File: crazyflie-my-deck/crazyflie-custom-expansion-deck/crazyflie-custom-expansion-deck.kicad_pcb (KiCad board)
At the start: 2 copper layers, 28 x 16 mm, 3 parts, among them J1 Conn_01x10, J2 Conn_02x10_Odd_Even, J3 Conn_01x10

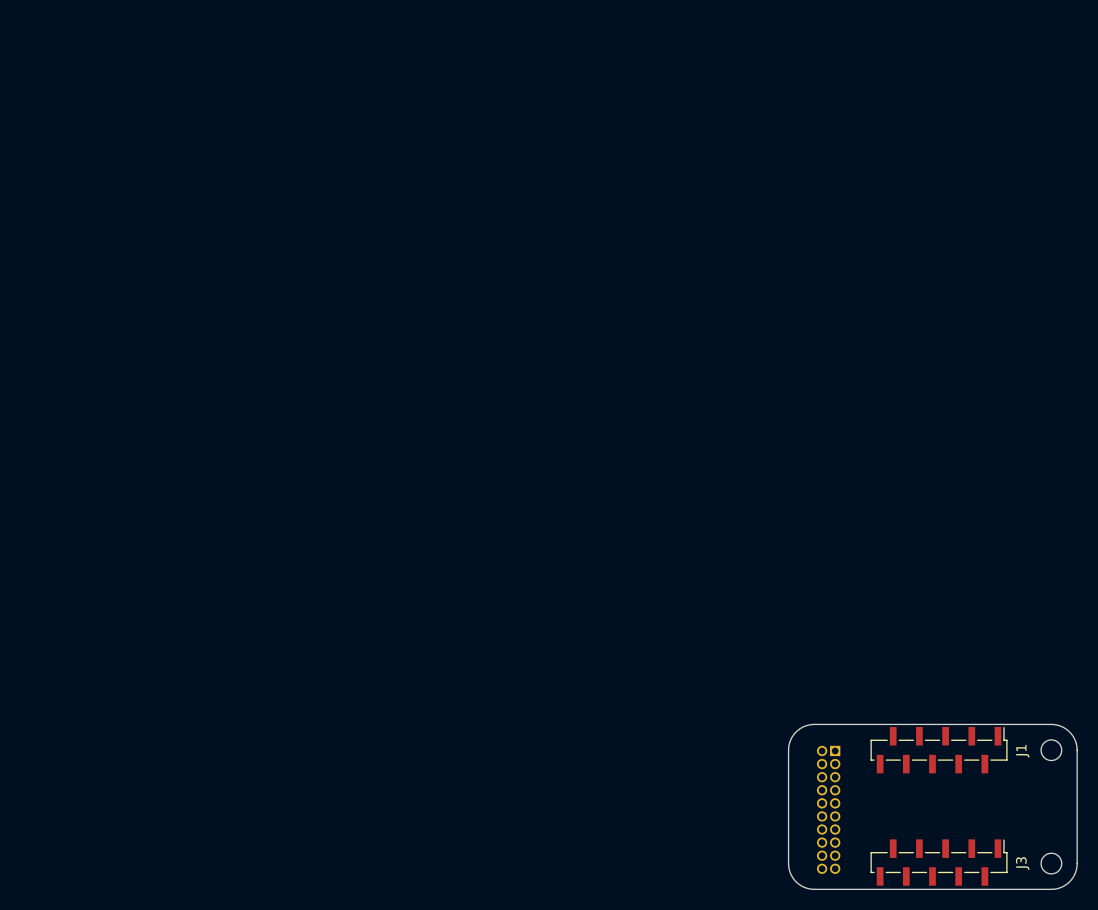
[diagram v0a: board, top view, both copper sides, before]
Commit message: [add] boost voltage
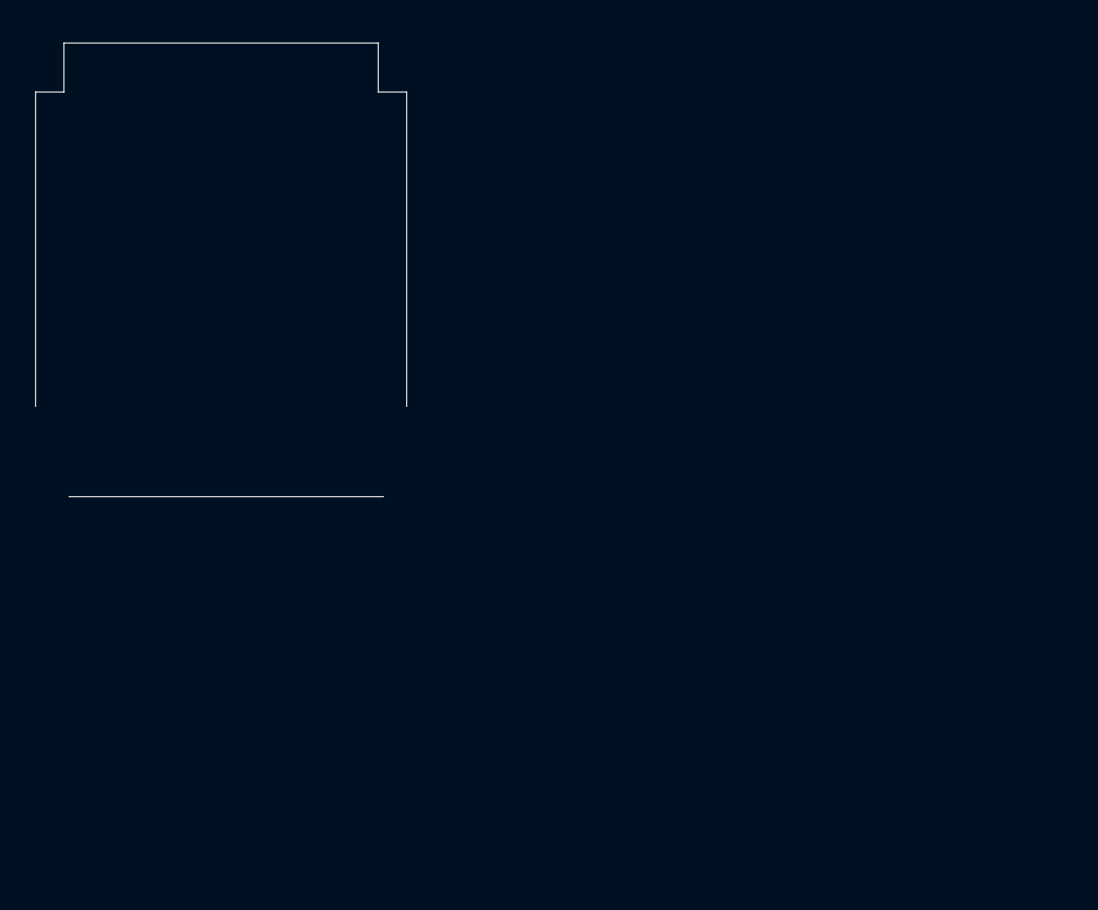
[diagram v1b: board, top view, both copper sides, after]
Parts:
- removed J1, J3: Conn_01x10, Connector_PinSocket_1.27mm:PinSocket_1x10_P1.27mm_Vertical_SMD_Pin1Left
- removed J2: Conn_02x10_Odd_Even, Connector_PinHeader_1.27mm:PinHeader_2x10_P1.27mm_Vertical
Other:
- board size 28 x 16 mm -> 36 x 44 mm

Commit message: acomodo de componentes
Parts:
- added C1: C_Polarized, Capacitor_Tantalum_SMD:CP_EIA-3528-15_AVX-H, F.Cu at (63.8, 35.0)
- added C2: C_Polarized, Capacitor_SMD:C_0805_2012Metric, F.Cu at (82.7, 52.0)
- added C3: C_Polarized, Capacitor_SMD:C_1210_3225Metric, F.Cu at (62.2, 52.0)
- added C4: C_Polarized, Capacitor_Tantalum_SMD:CP_EIA-3528-15_AVX-H, F.Cu at (77.5, 35.2)
- added D1: 1SS355VM, Diode_SMD:D_SOD-323F, F.Cu at (76.2, 40.0)
- added J1: Conn_01x10, Connector_PinSocket_1.27mm:PinSocket_1x10_P1.27mm_Vertical_SMD_Pin1Left, F.Cu at (56.8, 41.5)
- added J2: Conn_01x06_Male, Connector_PinHeader_1.27mm:PinHeader_1x06_P1.27mm_Horizontal, F.Cu at (68.2, 29.7)
- added J3: Conn_01x10, Connector_PinSocket_1.27mm:PinSocket_1x10_P1.27mm_Vertical_SMD_Pin1Left, F.Cu at (83.5, 41.5)
- added L1: L, Inductor_SMD:L_1210_3225Metric, F.Cu at (70.8, 34.8)
- added R1: R, Resistor_SMD:R_0805_2012Metric, F.Cu at (62.7, 40.5)
- added R2: R, Resistor_SMD:R_0805_2012Metric, F.Cu at (62.5, 43.5)
- added R3: R, Resistor_SMD:R_0805_2012Metric, F.Cu at (77.7, 49.2)
- added R4: R, Resistor_SMD:R_0805_2012Metric, F.Cu at (77.8, 51.8)
- added U1: MAX712CSE, Package_SO:SOIC-16_3.9x9.9mm_P1.27mm, F.Cu at (70.0, 43.0)
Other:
- board size 36 x 44 mm -> 36.2 x 37.7 mm

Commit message: Fixes
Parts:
- C1, C4: value C_Polarized -> 100uF
- C2: value C_Polarized -> 0.1uF
- C3: value C_Polarized -> 10uF
- R1: value R -> 120k
- R2: value R -> 30k
- R3: value R -> 390k
- R4: value R -> 130k
- U1: value MAX712CSE -> MAX7111
- moved C2 9.04 mm to (76.2, 45.7), turned to 90 degrees
- moved R3 7.74 mm to (73.7, 55.9), turned to -90 degrees
- moved R2 4.76 mm to (62.5, 48.3)
- moved R4 4.25 mm to (78.7, 55.9), turned to 90 degrees
- moved U1 3.07 mm to (68.6, 45.7)
- moved C3 2.41 mm to (62.2, 54.4)
- moved R1 1.71 mm to (61.0, 40.6)
- moved D1 0.64 mm to (76.2, 40.6)
- moved J2 0.35 mm to (68.6, 29.7)
- renumbered L1 to 22uH1
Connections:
- 22uH1 pad 2: Net-(D1-Pad2) -> Net-(22uH1-Pad2)
- C2 pad 1: unconnected-(C2-Pad1) -> Net-(C2-Pad1)
- C3 pad 1: unconnected-(C3-Pad1) -> Net-(C3-Pad1)
- D1 pad 2: Net-(D1-Pad2) -> Net-(22uH1-Pad2)
- R3 pad 1: unconnected-(R3-Pad1) -> Net-(C3-Pad1)
- U1 pad 1: unconnected-(U1-Pad1) -> Net-(22uH1-Pad2)
- U1 pad 10: unconnected-(U1-Pad10) -> Net-(C2-Pad1)
- U1 pad 11: unconnected-(U1-Pad11) -> Net-(R1-Pad2)
- U1 pad 12: unconnected-(U1-Pad12) -> Net-(C4-Pad1)
- U1 pad 13: unconnected-(U1-Pad13) -> Net-(C2-Pad1)
- U1 pad 14: unconnected-(U1-Pad14) -> GND
- U1 pad 15: unconnected-(U1-Pad15) -> GND
- U1 pad 16: unconnected-(U1-Pad16) -> Net-(22uH1-Pad2)
- U1 pad 2: unconnected-(U1-Pad2) -> GND
- U1 pad 3: unconnected-(U1-Pad3) -> GND
- U1 pad 4: unconnected-(U1-Pad4) -> Net-(C4-Pad1)
- U1 pad 5: unconnected-(U1-Pad5) -> Net-(C4-Pad1)
- U1 pad 6: unconnected-(U1-Pad6) -> Net-(R3-Pad2)
- U1 pad 7: unconnected-(U1-Pad7) -> Net-(C4-Pad1)
- U1 pad 9: unconnected-(U1-Pad9) -> Net-(C3-Pad1)
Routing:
- net GND: track 0.00 -> 26.9 mm
- net Net-(R1-Pad2): track 0.00 -> 10.6 mm
- net Net-(C3-Pad1): track 0.00 -> 7.04 mm
- net Net-(22uH1-Pad1): track 0.00 -> 6.54 mm
- net Net-(R3-Pad2): track 0.00 -> 5.08 mm

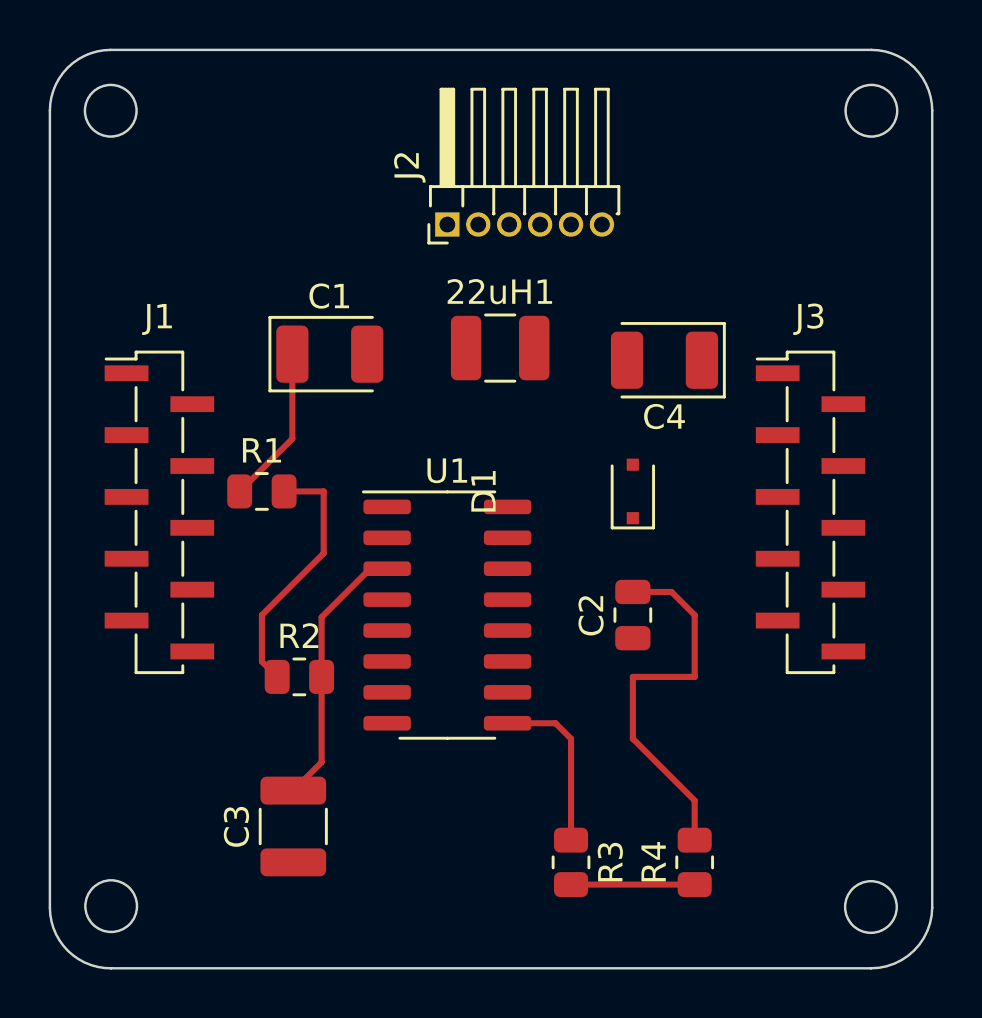
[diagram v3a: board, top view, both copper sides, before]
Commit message: Tracks - voltage boost
Falta 1 y las tracks a GND
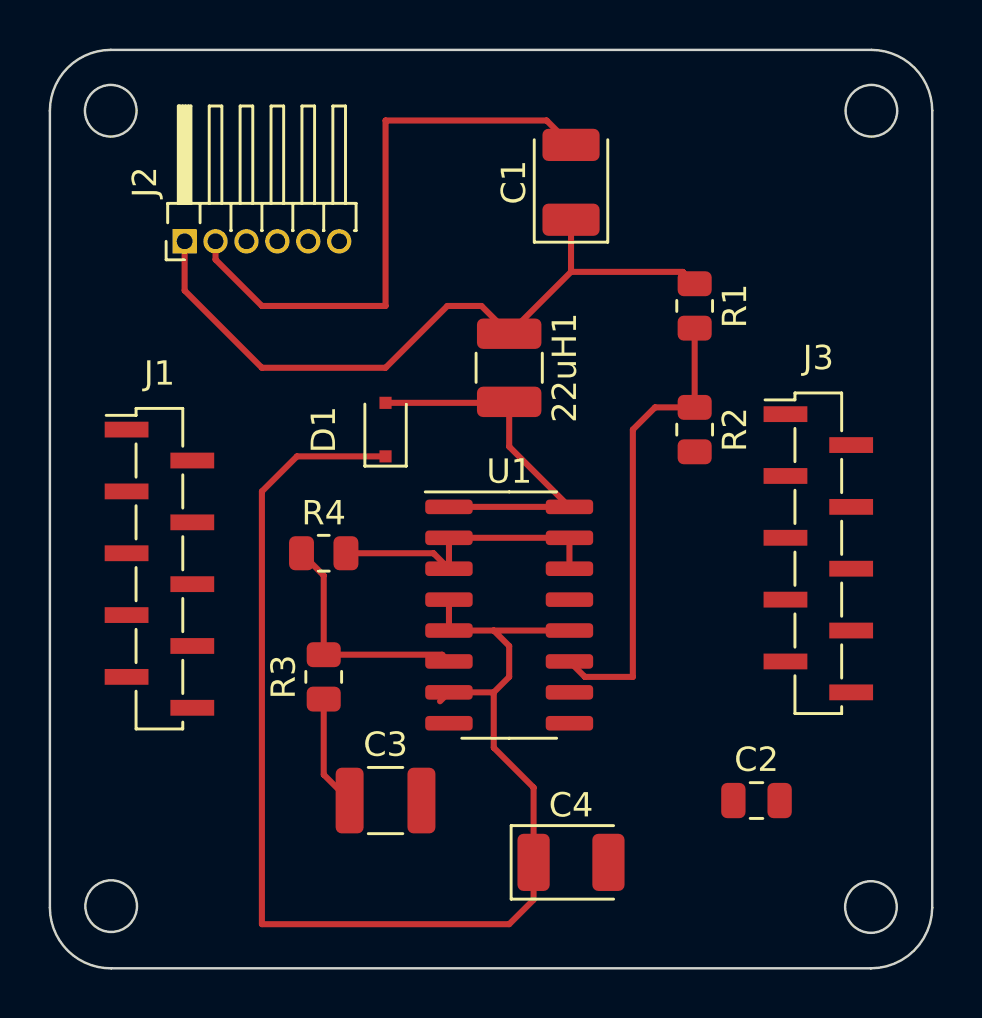
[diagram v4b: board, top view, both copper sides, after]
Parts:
- moved C4 21.0 mm to (73.7, 55.9), turned to 0 degrees
- moved R4 19.8 mm to (63.5, 43.2), turned to 0 degrees
- moved R1 19.3 mm to (78.7, 33.0), turned to -90 degrees
- moved R2 19.2 mm to (78.7, 38.1), turned to -90 degrees
- moved R3 12.7 mm to (63.5, 48.3), turned to 90 degrees
- moved C1 12.2 mm to (73.7, 27.9), turned to 90 degrees
- moved J2 10.8 mm to (57.8, 30.4)
- moved D1 10.5 mm to (66.0, 38.1)
- moved C2 9.16 mm to (81.3, 53.3), turned to 0 degrees
- moved C3 3.94 mm to (66.0, 53.3), turned to 0 degrees
- moved U1 2.54 mm to (71.1, 45.7)
- moved J1 2.31 mm to (56.8, 43.8)
- moved J3 1.71 mm to (83.8, 43.2)
- moved 22uH1 0.89 mm to (71.1, 35.6), turned to -90 degrees
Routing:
- net Net-(C4-Pad1): track 0.00 -> 55.9 mm
- net Net-(22uH1-Pad1): track 6.54 -> 29.2 mm
- net Net-(22uH1-Pad2): track 0.00 -> 15.4 mm
- net GND: track 26.9 -> 36.2 mm
- net Net-(R1-Pad2): track 10.6 -> 19.2 mm
- net Net-(R3-Pad2): track 5.08 -> 9.81 mm
- net Net-(C3-Pad1): track 7.04 -> 4.61 mm

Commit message: Update
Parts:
- C2, R2: moved to B.Cu
- turned C2 to -90 degrees
- turned R2 to 180 degrees
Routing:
- net (no net): track 0.00 -> 18.6 mm, vias 0 -> 3
- net Net-(R1-Pad2): track 19.2 -> 5.41 mm
- added copper zone on B.Cu, net GND
